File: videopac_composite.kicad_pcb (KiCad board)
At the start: 2 copper layers, 61.1 x 23.9 mm, 17 parts, among them J102 Composite Output, J104 Composite Input, Q101 BC548, Q102 BC558, Q103 BC548

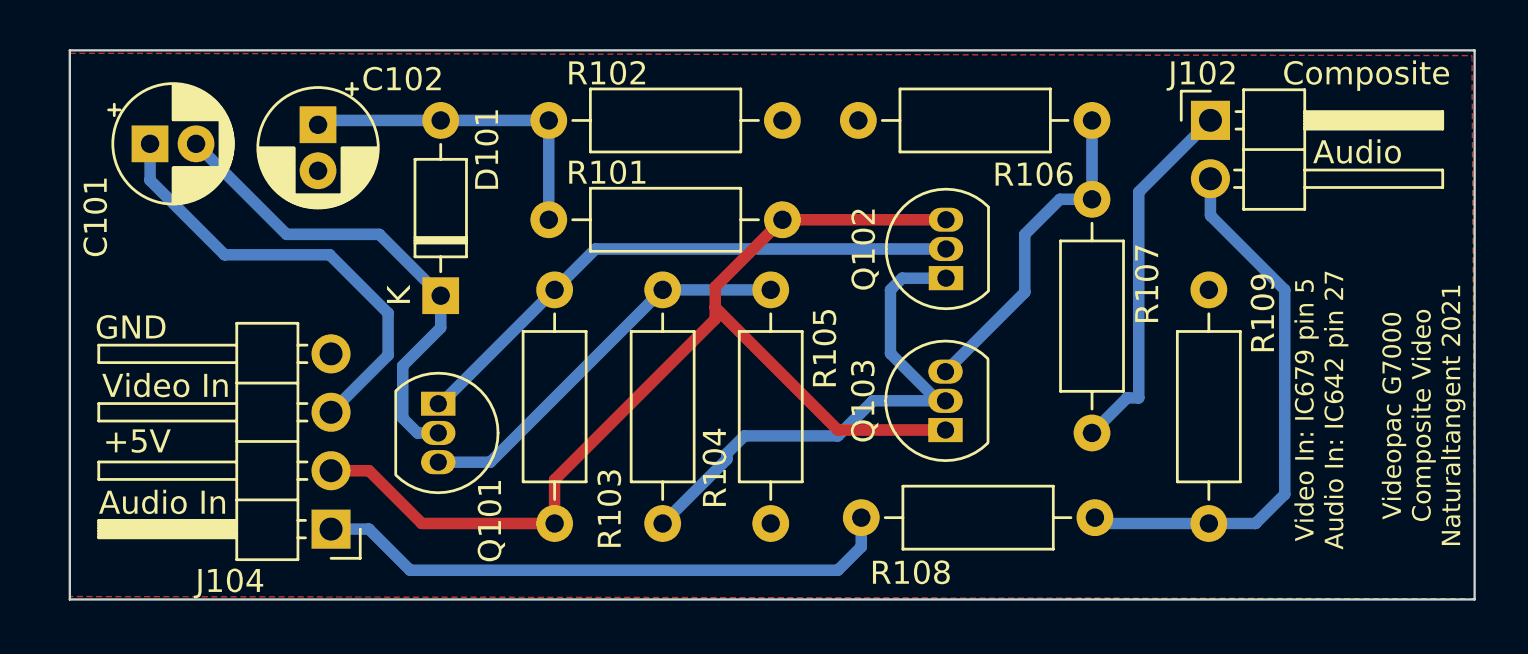
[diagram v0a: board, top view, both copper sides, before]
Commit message: Add additional ground connections.
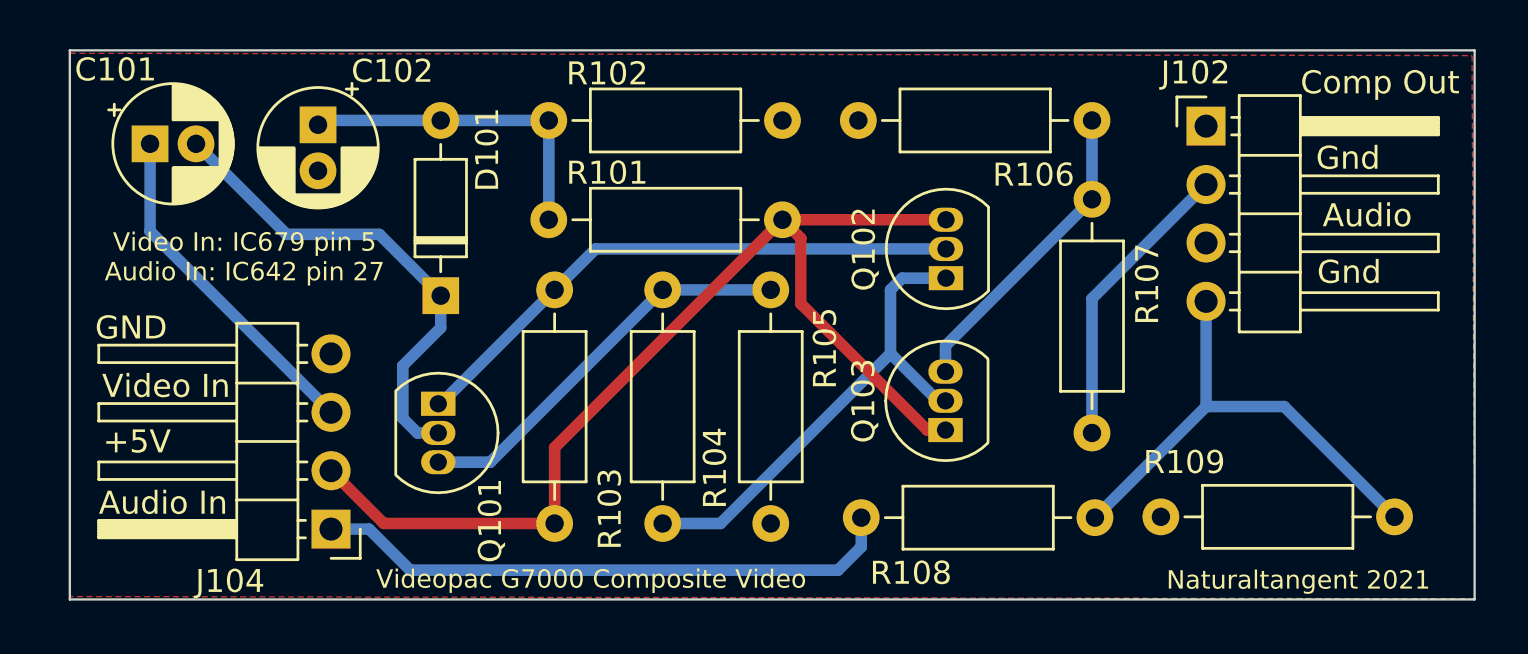
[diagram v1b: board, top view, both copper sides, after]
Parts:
- J102: value Composite Output -> Conn_01x04; footprint Connector_PinHeader_2.54mm:PinHeader_1x02_P2.54mm_Horizontal -> Connector_PinHeader_2.54mm:PinHeader_1x04_P2.54mm_Horizontal
- moved R109 10.1 mm to (77.3, 80.6), turned to 0 degrees
- moved J102 0.32 mm to (79.3, 63.6)
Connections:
- J102 pad 1: COMPOSITE OUTPUT -> GND
- J102 pad 2: AUDIO OUTPUT -> COMPOSITE OUTPUT
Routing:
- net VIDEO INPUT: track 19.7 -> 14.9 mm
- net COMPOSITE OUTPUT: track 16.0 -> 12.9 mm
- net AUDIO OUTPUT: track 23.9 -> 21.6 mm
- net Net-(Q102-Pad1): track 23.3 -> 21.6 mm
- net Net-(Q103-Pad3): track 14.4 -> 13.6 mm
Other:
- board text added: "Comp Out"
- board text added: "Gnd"
- board text added: "Naturaltangent 2021"
- board text added: "Videopac G7000 Composite Video"
- board text removed: "Composite"
- board text removed: "Videopac G7000 Composite Video Naturaltangent 2021"
